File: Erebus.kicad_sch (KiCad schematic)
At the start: 78 parts, among them J1 MJ-4PP-9, SW1 SW_PUSH-MX_W_LED, SW10 SW_PUSH-MX_W_LED, SW11 SW_PUSH-MX_W_LED, SW12 SW_PUSH-MX_W_LED, SW13 SW_PUSH-MX_W_LED, SW14 SW_PUSH-MX_W_LED, SW15 SW_PUSH-MX_W_LED, SW16 SW_PUSH-MX_W_LED, SW17 SW_PUSH-MX_W_LED, SW18 RotaryEncoder_Switch, SW19 SW_PUSH-MX_W_LED, SW2 SW_PUSH-MX_W_LED, SW20 SW_PUSH-MX_W_LED, SW21 SW_PUSH-MX_W_LED, SW22 SW_PUSH-MX_W_LED, SW23 SW_PUSH-MX_W_LED, SW24 SW_PUSH-MX_W_LED, SW25 SW_PUSH-MX_W_LED, SW26 SW_PUSH-MX_W_LED, SW27 SW_PUSH-MX_W_LED, SW3 SW_PUSH-MX_W_LED, SW4 SW_PUSH-MX_W_LED, SW5 SW_PUSH-MX_W_LED, SW6 SW_PUSH-MX_W_LED, SW7 SW_PUSH-MX_W_LED, SW8 SW_PUSH-MX_W_LED, SW9 SW_PUSH-MX_W_LED, U1 ProMicro

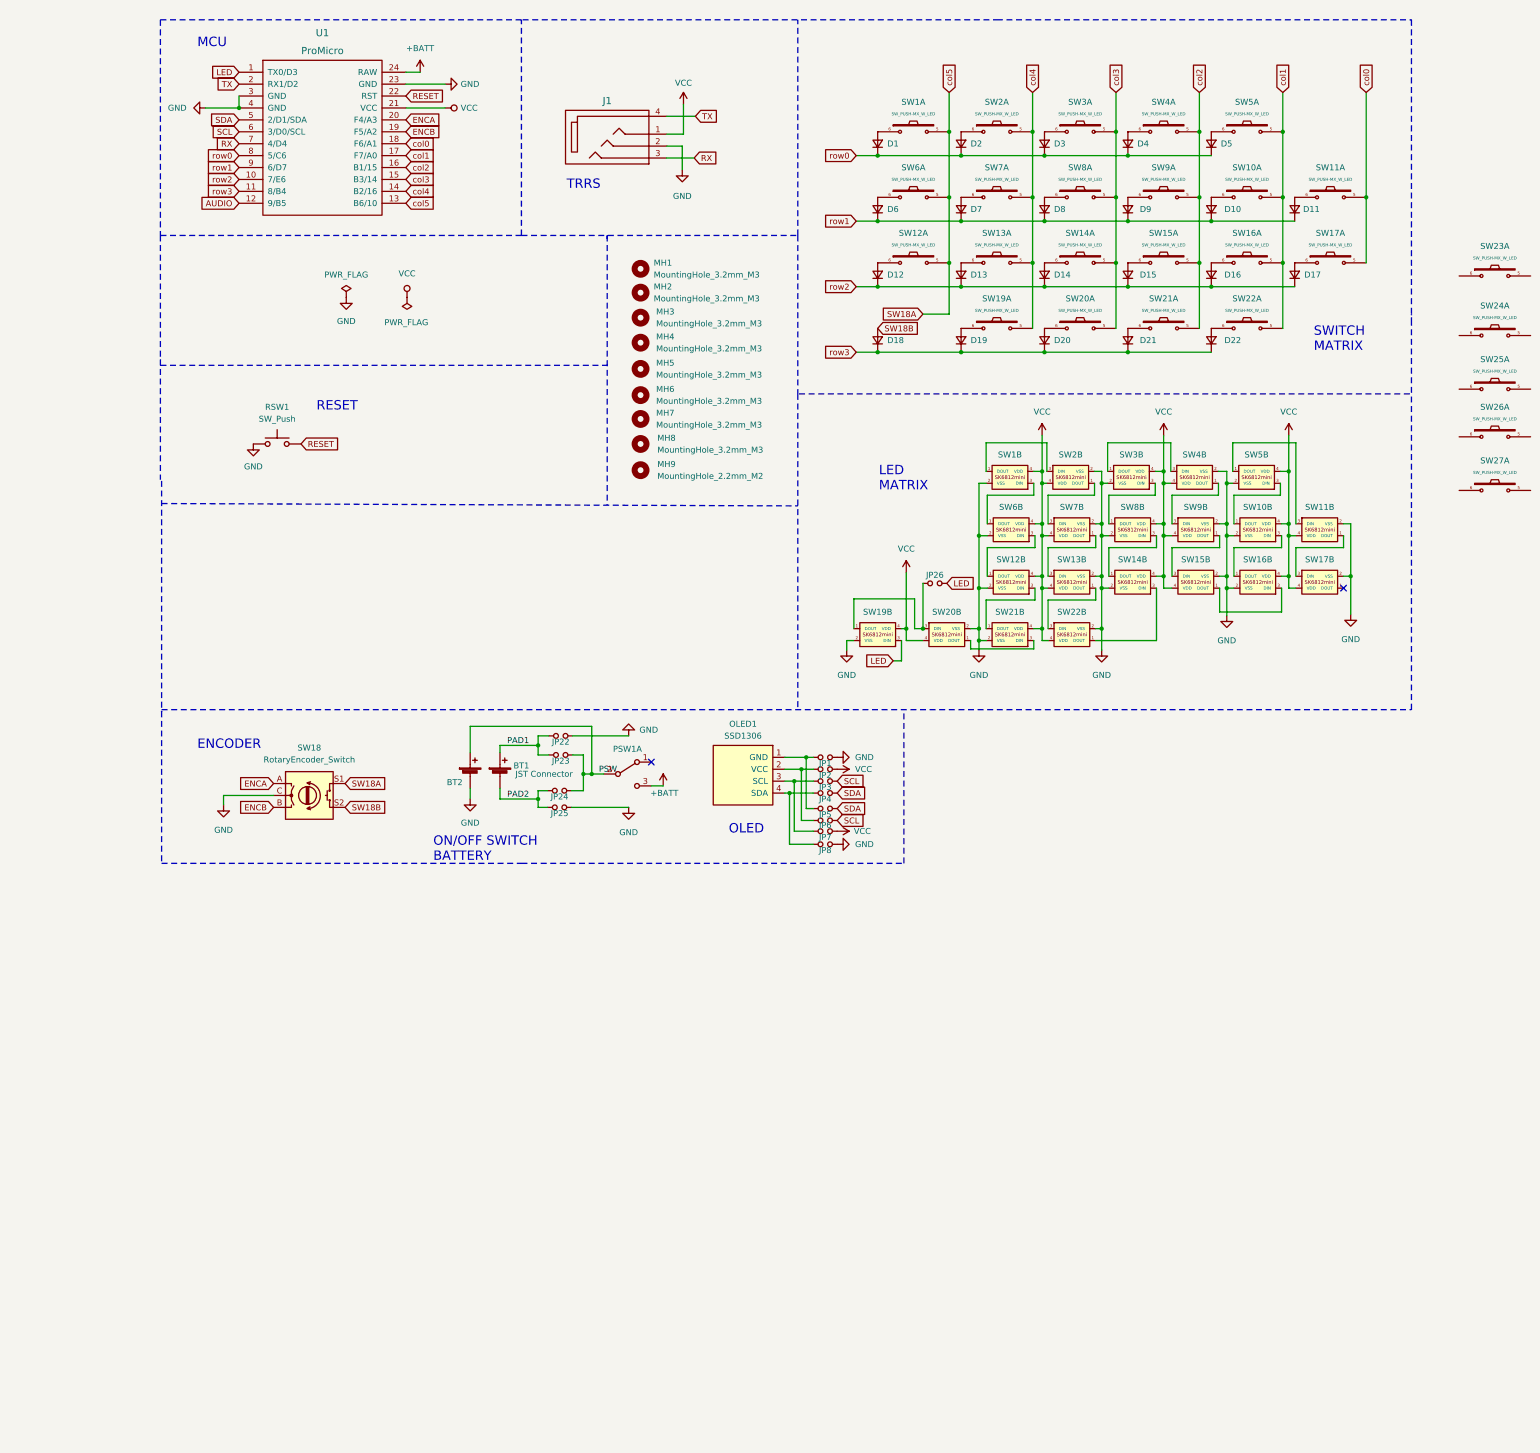
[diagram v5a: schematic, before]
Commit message: Added and finalized layout of switches
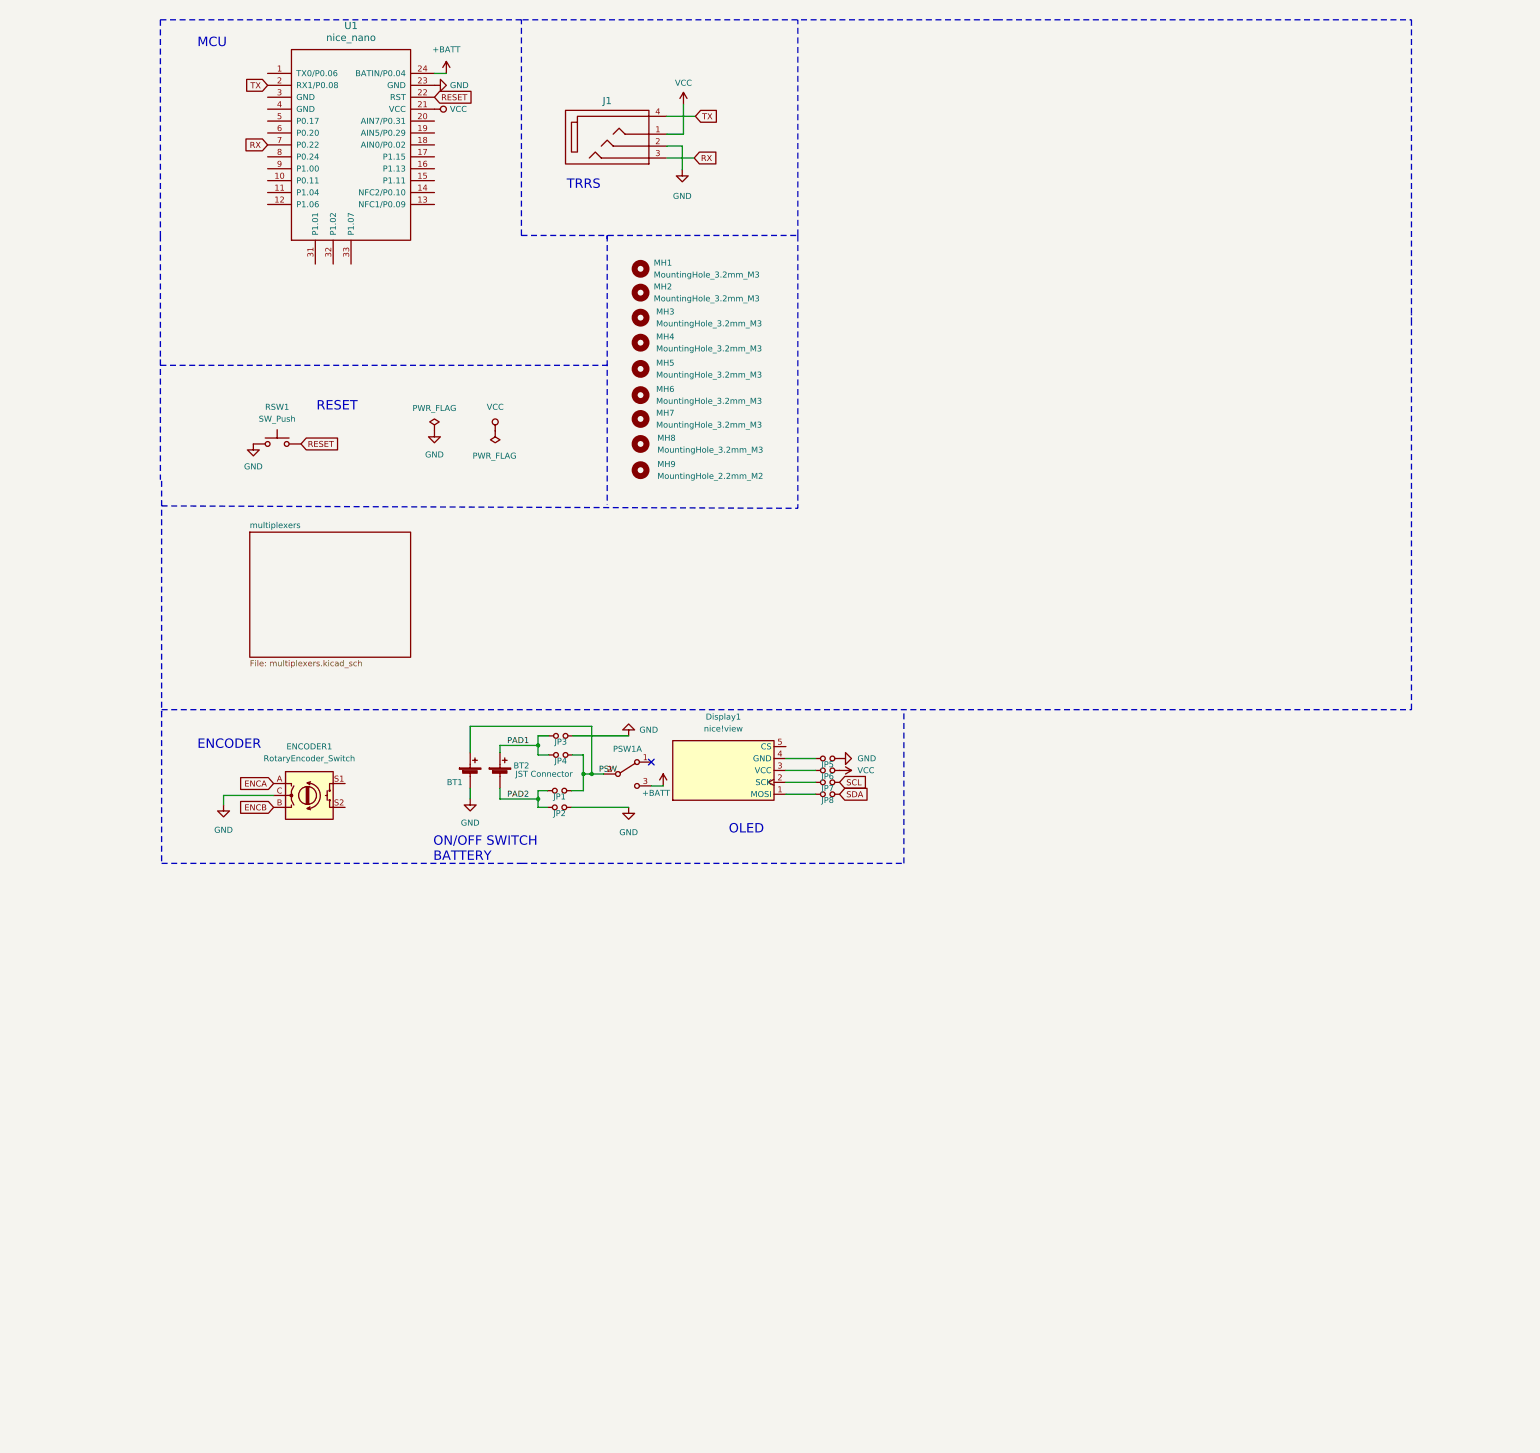
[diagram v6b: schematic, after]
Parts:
- removed D1, D10, D11, D12, D13, D14, D15, D16, D17, D18, D19, D2, D20, D21, D22, D3, D4, D5, D6, D7, D8, D9: D_Small, KLOR:Diode_SOD123, symbol Device:D_Small
- removed JP26, JP5, JP6, JP7, JP8: Device_Jumper_NO_Small, KLOR:Jumper, symbol KLORlib:Device_Jumper_NO_Small
- removed OLED1: SSD1306, KLOR:SSD1306_128x64OLED, symbol SSD1306-128x64_OLED:SSD1306
- removed SW1, SW10, SW11, SW12, SW13, SW14, SW15, SW16, SW17, SW19, SW2, SW20, SW21, SW22, SW23, SW24, SW25, SW26, SW27, SW3, SW4, SW5, SW6, SW7, SW8, SW9: SW_PUSH-MX_W_LED, KLOR:SK6812MINI_and_cherry, symbol KLORlib:SW_PUSH-MX_W_LED
- removed U1: ProMicro, KLOR:ProMicro, symbol Buzzard:ProMicro
- added Display1: nice!view, EREBUS:nice_view, symbol EREBUSlib:nice!view
- added U1: nice_nano, EREBUS:nice_nano, symbol EREBUSlib:nice_nano
- BT1: renamed from BT2; footprint KLOR:custombatteryconnector_small -> EREBUS:custombatteryconnector_small
- BT2: renamed from BT1; footprint KLOR:JST_PH_reversible -> EREBUS:JST_PH_reversible
- ENCODER1: renamed from SW18; footprint KLOR:RotaryEncoder_Alps_EC11E-Switch_Vertical_H20mm-keebio_modified -> EREBUS:RotaryEncoder_Alps_EC11E-Switch_Vertical_H20mm-keebio_modified
- J1: footprint KLOR:MJ-4PP-9 -> EREBUS:MJ-4PP-9
- JP1: renamed from JP24; footprint KLOR:Jumper -> EREBUS:Jumper
- JP2: renamed from JP25; footprint KLOR:Jumper -> EREBUS:Jumper
- JP3: renamed from JP22; footprint KLOR:Jumper -> EREBUS:Jumper
- JP4: renamed from JP23; footprint KLOR:Jumper -> EREBUS:Jumper
- JP5: renamed from JP1; footprint KLOR:Jumper -> EREBUS:Jumper
- JP6: renamed from JP2; footprint KLOR:Jumper -> EREBUS:Jumper
- JP7: renamed from JP3; footprint KLOR:Jumper -> EREBUS:Jumper
- JP8: renamed from JP4; footprint KLOR:Jumper -> EREBUS:Jumper
- PSW1: footprint KLOR:MSK12C02_reversible -> EREBUS:MSK12C02_reversible
- RSW1: footprint KLOR:SW_Push_1P1T-MP_NO_Horizontal_Alps_SKRTLAE010_both_sides -> EREBUS:SW_Push_1P1T-MP_NO_Horizontal_Alps_SKRTLAE010_both_sides
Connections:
- net +BATT: now also U1.24 (BATIN/P0.04)
- net GND: now also U1.23 (GND)
- net RESET: now also U1.22 (RST)
- net RX: now also U1.7 (P0.22)
- net TX: now also U1.2 (RX1/P0.08)
- net VCC: now also U1.21 (VCC)
- net at JP5.1: now also Display1.4 (GND)
- net at JP6.1: now also Display1.3 (VCC)
- net at JP7.1: now also Display1.2 (SCK)
- net at JP8.1: now also Display1.1 (MOSI)
- net SW18A: no longer names the net of ENCODER1.S1
- net SW18B: no longer names the net of ENCODER1.S2
- no-connect marks 2 -> 1
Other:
- added sheet multiplexers (multiplexers.kicad_sch)
- note removed: "LED MATRIX"
- note removed: "SWITCH MATRIX"
- moved on the sheet: JP5, JP6, JP7, JP8
